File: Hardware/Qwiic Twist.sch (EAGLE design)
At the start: 41 parts, among them J3 PTH, J7 ISP, SW1 Rotary Encoder, U4 ATTINY84-ARDUINO

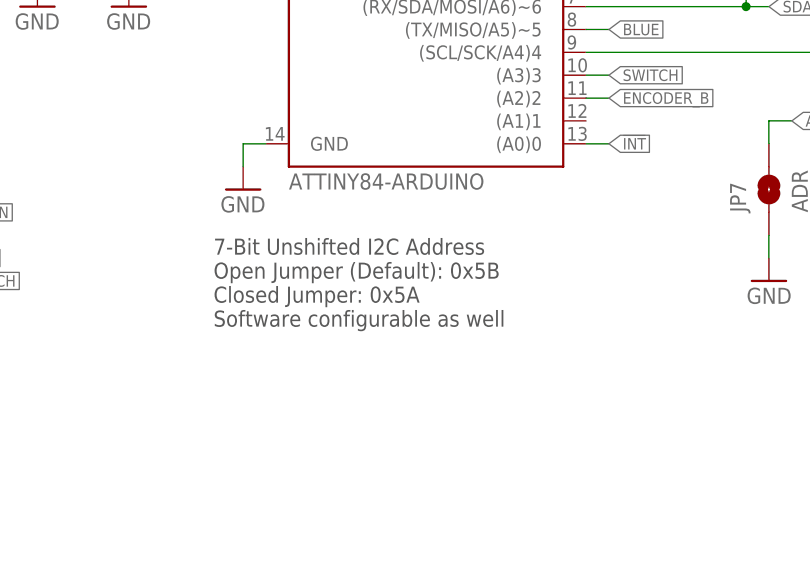
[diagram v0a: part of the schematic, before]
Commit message: Adding ignore. Fix I2C addresses in schematic. Add dims and new sch pdfs.
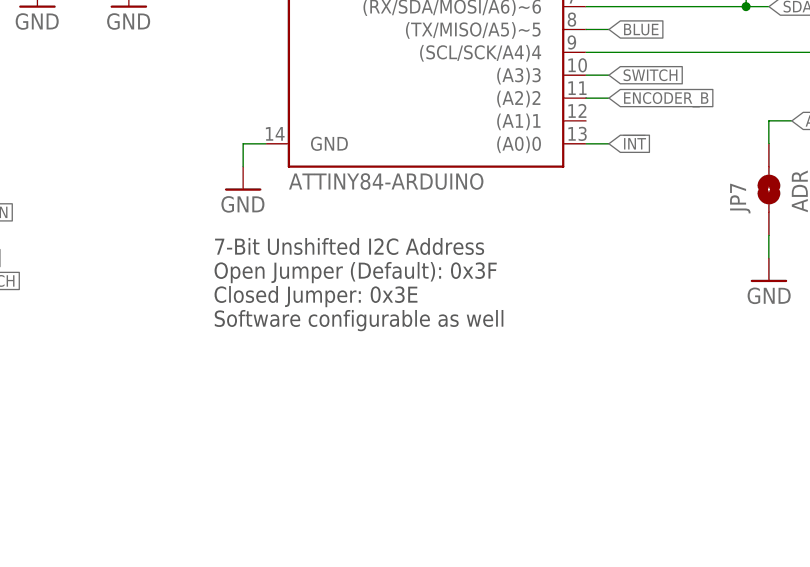
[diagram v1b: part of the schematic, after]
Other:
- note added: "7-Bit Unshifted I2C Address Open Jumper (Default): 0x3F Closed Jumper: 0x3E Software configurable as well"
- note removed: "7-Bit Unshifted I2C Address Open Jumper (Default): 0x5B Closed Jumper: 0x5A Software configurable as well"
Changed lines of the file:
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@@
 <?xml version="1.0" encoding="utf-8"?>
 <!DOCTYPE eagle SYSTEM "eagle.dtd">
-<eagle version="9.2.1">
+<eagle version="9.4.0">
 <drawing>
 <settings>
@@
 <text x="237.744" y="7.366" size="2.54" layer="94">X10</text>
 <text x="156.718" y="99.06" size="1.778" layer="97">7-Bit Unshifted I2C Address
-Open Jumper (Default): 0x5B
-Closed Jumper: 0x5A
+Open Jumper (Default): 0x3F
+Closed Jumper: 0x3E
 Software configurable as well</text>
 <text x="215.773" y="164.211" size="1.778" layer="97">I2C Pull Ups</text>
